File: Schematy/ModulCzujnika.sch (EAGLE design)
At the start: 10 parts, among them X1 GLX-S-88M

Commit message: Dodanie podciągającego rezystora na wyjście lm393
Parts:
- added R1: 10k, rcl:R-EU_0207/7
- R12: value 100k -> 10k
- R13: value 1k -> 5k
- R14: value 1k -> 10k
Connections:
- net N$24: now also R1.2
- net VCC: now also R1.1
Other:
- moved on the sheet: LED3, R14, R15, SW2, U$7, X1

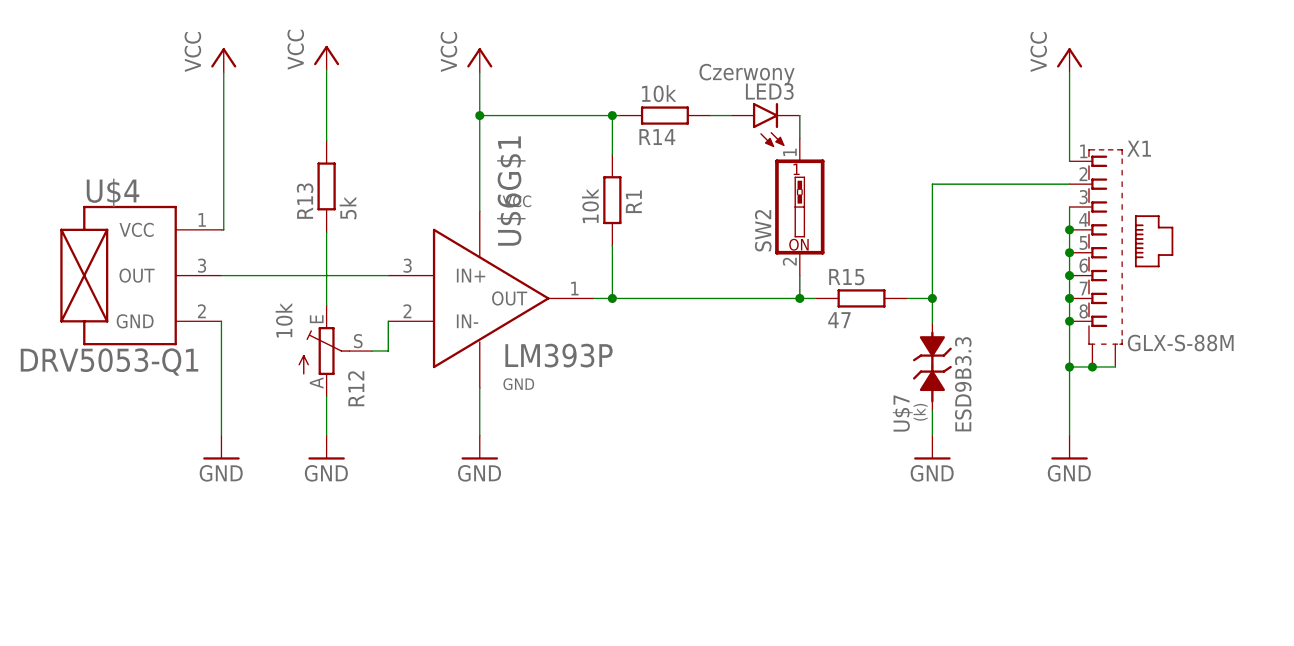
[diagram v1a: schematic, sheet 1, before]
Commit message: Częściowe zabezpieczenie modułu czujnika
Częściowe zabezpieczenie modułu czujnika przed nagłym wzrostem napięcia na wejściu modułu.
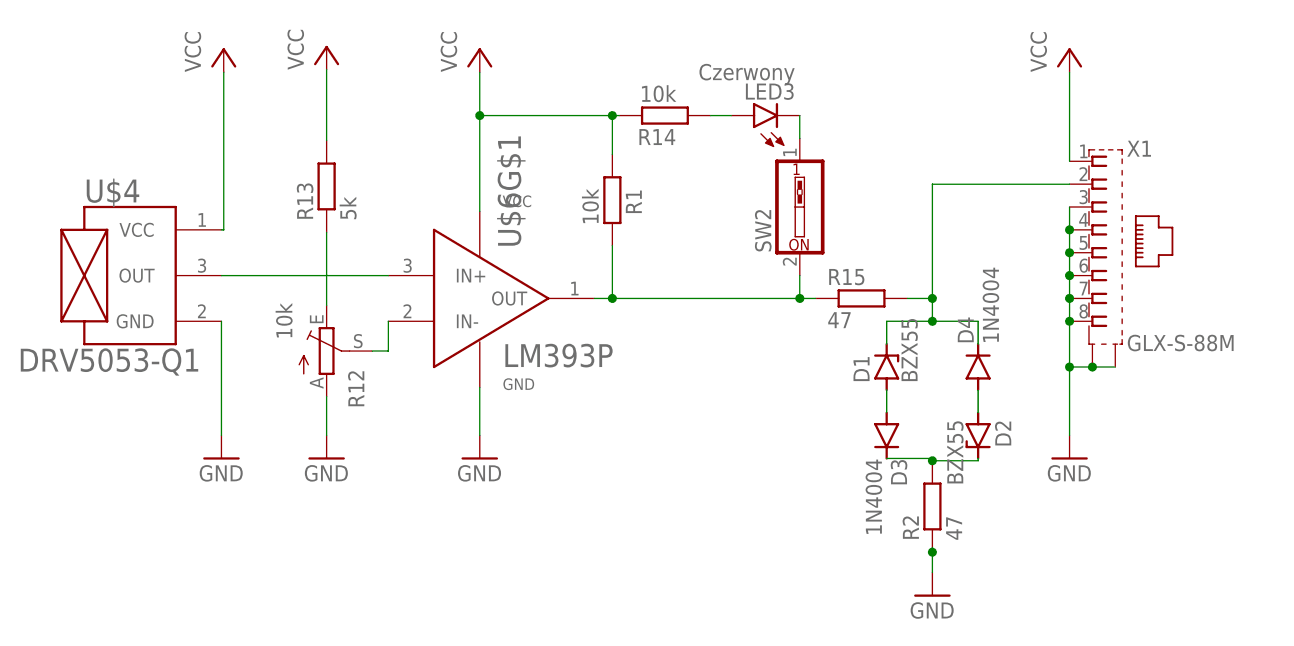
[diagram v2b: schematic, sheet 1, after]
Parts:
- removed U$7: ESD9B3.3, BezkonataktowyLicznikObrotów:ESD9B3.3
- added D1, D2: BZX55, diode:BZX55
- added D3, D4: 1N4004, diode:1N4004
- added R2: 47, rcl:R-EU_0207/7
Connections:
- new net N$1: D2.C, D3.C, R2.2
- new net N$3: D2.A, D4.A
- new net N$4: D1.A, D3.A
- net GND: now also R2.1; no longer U$7.K
- net N$2: now also D1.C, D4.C; no longer U$7.A
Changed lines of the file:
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@@
 <part name="LED3" library="led" library_urn="urn:adsk.eagle:library:259" deviceset="LED" device="5MM" package3d_urn="urn:adsk.eagle:package:15799/2" value="Czerwony"/>
 <part name="R15" library="rcl" library_urn="urn:adsk.eagle:library:334" deviceset="R-EU_" device="0207/7" package3d_urn="urn:adsk.eagle:package:23493/2" value="47"/>
-<part name="U$7" library="BezkonataktowyLicznikObrotów" deviceset="ESD9B3.3" device=""/>
 <part name="X1" library="con-kycon" library_urn="urn:adsk.eagle:library:157" deviceset="GLX-S-88M" device="" package3d_urn="urn:adsk.eagle:package:7680/1"/>
 <part name="P+1" library="supply1" library_urn="urn:adsk.eagle:library:371" deviceset="VCC" device=""/>
@@
 <part name="FRAME1" library="frames" library_urn="urn:adsk.eagle:library:229" deviceset="DINA5_L" device=""/>
 <part name="R1" library="rcl" library_urn="urn:adsk.eagle:library:334" deviceset="R-EU_" device="0207/7" package3d_urn="urn:adsk.eagle:package:23493/2" value="10k"/>
+<part name="R2" library="rcl" library_urn="urn:adsk.eagle:library:334" deviceset="R-EU_" device="0207/7" package3d_urn="urn:adsk.eagle:package:23493/2" value="47"/>
+<part name="D1" library="diode" library_urn="urn:adsk.eagle:library:210" deviceset="BZX55" device="" package3d_urn="urn:adsk.eagle:package:43342/1"/>
+<part name="D2" library="diode" library_urn="urn:adsk.eagle:library:210" deviceset="BZX55" device="" package3d_urn="urn:adsk.eagle:package:43342/1"/>
+<part name="D3" library="diode" library_urn="urn:adsk.eagle:library:210" deviceset="1N4004" device="" package3d_urn="urn:adsk.eagle:package:43336/1"/>
+<part name="D4" library="diode" library_urn="urn:adsk.eagle:library:210" deviceset="1N4004" device="" package3d_urn="urn:adsk.eagle:package:43336/1"/>
 </parts>
 <sheets>
@@
 <attribute name="VALUE" x="-4.572" y="-20.32" size="1.778" layer="96"/>
 </instance>
-<instance part="GND16" gate="1" x="48.26" y="-17.78" smashed="yes">
-<attribute name="VALUE" x="45.72" y="-20.32" size="1.778" layer="96"/>
+<instance part="GND16" gate="1" x="48.26" y="-33.02" smashed="yes">
+<attribute name="VALUE" x="45.72" y="-35.56" size="1.778" layer="96"/>
 </instance>
 <instance part="SW2" gate="G$1" x="33.528" y="10.16" smashed="yes" rot="R90">
@@
 <attribute name="NAME" x="36.576" y="1.4986" size="1.778" layer="95"/>
 <attribute name="VALUE" x="36.576" y="-3.302" size="1.778" layer="96"/>
-</instance>
-<instance part="U$7" gate="G$1" x="48.26" y="-7.366" smashed="yes" rot="R90">
-<attribute name="VALUE" x="52.578" y="-14.986" size="1.778" layer="95" rot="R90"/>
-<attribute name="NAME" x="45.72" y="-14.986" size="1.778" layer="95" rot="R90"/>
 </instance>
 <instance part="X1" gate="G$1" x="66.04" y="5.08" smashed="yes">
@@
 <attribute name="NAME" x="14.1986" y="12.192" size="1.778" layer="95" rot="R270"/>
 <attribute name="VALUE" x="9.398" y="12.192" size="1.778" layer="96" rot="R270"/>
+</instance>
+<instance part="R2" gate="G$1" x="48.26" y="-23.114" smashed="yes" rot="R90">
+<attribute name="NAME" x="46.7614" y="-26.924" size="1.778" layer="95" rot="R90"/>
+<attribute name="VALUE" x="51.562" y="-26.924" size="1.778" layer="96" rot="R90"/>
+</instance>
+<instance part="D1" gate="1" x="43.18" y="-7.62" smashed="yes" rot="R90">
+<attribute name="NAME" x="41.275" y="-9.398" size="1.778" layer="95" rot="R90"/>
+<attribute name="VALUE" x="46.609" y="-9.398" size="1.778" layer="96" rot="R90"/>
+</instance>
+<instance part="D2" gate="1" x="53.34" y="-15.24" smashed="yes" rot="R270">
+<attribute name="NAME" x="55.245" y="-13.462" size="1.778" layer="95" rot="R270"/>
+<attribute name="VALUE" x="49.911" y="-13.462" size="1.778" layer="96" rot="R270"/>
+</instance>
+<instance part="D3" gate="1" x="43.18" y="-15.24" smashed="yes" rot="R270">
+<attribute name="NAME" x="43.6626" y="-17.78" size="1.778" layer="95" rot="R270"/>
+<attribute name="VALUE" x="40.8686" y="-17.78" size="1.778" layer="96" rot="R270"/>
+</instance>
+<instance part="D4" gate="1" x="53.34" y="-7.62" smashed="yes" rot="R90">
+<attribute name="NAME" x="52.8574" y="-5.08" size="1.778" layer="95" rot="R90"/>
+<attribute name="VALUE" x="55.6514" y="-5.08" size="1.778" layer="96" rot="R90"/>
 </instance>
 </instances>
@@
 </segment>
 <segment>
-<wire x1="48.26" y1="-15.24" x2="48.26" y2="-12.446" width="0.1524" layer="91"/>
+<wire x1="48.26" y1="-30.48" x2="48.26" y2="-28.194" width="0.1524" layer="91"/>
 <pinref part="GND16" gate="1" pin="GND"/>
-<pinref part="U$7" gate="G$1" pin="K"/>
+<pinref part="R2" gate="G$1" pin="1"/>
+<wire x1="48.26" y1="-28.194" x2="48.26" y2="-27.686" width="0.1524" layer="91"/>
+<junction x="48.26" y="-28.194"/>
 </segment>
 <segment>
@@
 <wire x1="48.26" y1="12.7" x2="48.26" y2="0" width="0.1524" layer="91"/>
 <wire x1="45.466" y1="0" x2="48.26" y2="0" width="0.1524" layer="91"/>
-<wire x1="48.26" y1="-2.794" x2="48.26" y2="0" width="0.1524" layer="91"/>
+<wire x1="48.26" y1="-2.794" x2="48.26" y2="-2.54" width="0.1524" layer="91"/>
 <pinref part="R15" gate="G$1" pin="2"/>
-<pinref part="U$7" gate="G$1" pin="A"/>
 <junction x="48.26" y="0"/>
-</segment>
-</net>
+<pinref part="D1" gate="1" pin="C"/>
+<wire x1="48.26" y1="-2.54" x2="48.26" y2="0" width="0.1524" layer="91"/>
+<wire x1="43.18" y1="-5.08" x2="43.18" y2="-2.54" width="0.1524" layer="91"/>
+<wire x1="43.18" y1="-2.54" x2="48.26" y2="-2.54" width="0.1524" layer="91"/>
+<junction x="48.26" y="-2.54"/>
+<pinref part="D4" gate="1" pin="C"/>
+<wire x1="53.34" y1="-5.08" x2="53.34" y2="-2.54" width="0.1524" layer="91"/>
+<wire x1="53.34" y1="-2.54" x2="48.26" y2="-2.54" width="0.1524" layer="91"/>
+</segment>
+</net>
+<net name="N$1" class="0">
+<segment>
+<pinref part="D3" gate="1" pin="C"/>
+<pinref part="R2" gate="G$1" pin="2"/>
+<wire x1="43.18" y1="-17.78" x2="48.26" y2="-17.78" width="0.1524" layer="91"/>
+<wire x1="48.26" y1="-17.78" x2="48.26" y2="-18.034" width="0.1524" layer="91"/>
+<pinref part="D2" gate="1" pin="C"/>
+<wire x1="53.34" y1="-17.78" x2="53.34" y2="-18.034" width="0.1524" layer="91"/>
+<wire x1="53.34" y1="-18.034" x2="48.26" y2="-18.034" width="0.1524" layer="91"/>
+<junction x="48.26" y="-18.034"/>
+</segment>
+</net>
+<net name="N$3" class="0">
+<segment>
+<pinref part="D2" gate="1" pin="A"/>
+<pinref part="D4" gate="1" pin="A"/>
+<wire x1="53.34" y1="-12.7" x2="53.34" y2="-10.16" width="0.1524" layer="91"/>
+</segment>
+</net>
+<net name="N$4" class="0">
+<segment>
+<pinref part="D1" gate="1" pin="A"/>
+<pinref part="D3" gate="1" pin="A"/>
+<wire x1="43.18" y1="-10.16" x2="43.18" y2="-12.7" width="0.1524" layer="91"/>
+</segment>
+</net>
